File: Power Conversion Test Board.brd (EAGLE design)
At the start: 130 x 112.6 mm, 44 parts, among them U1 LM2678, U2 LM2678

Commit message: lots of things
put in board outline, also fixed the inductors because they were the wrong ones
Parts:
- removed L1, L2, L3, L4: 7.5uH, rcl:L2012C
- removed L5, L6: 15uH, rcl:L2012C
- added U$10, U$7, U$8, U$9: 7.8 uH, DiscreteComponents:HCMA1305
- added U$11, U$6: 15 uH, DiscreteComponents:HCMA1305
- moved U$3 119.1 mm to (78.7, 67.3)
- moved C28 116.3 mm to (72.4, 53.3)
- moved U2 115.6 mm to (44.5, 73.7)
- moved U$4 115.0 mm to (63.5, 92.7)
- moved U1 111.5 mm to (40.6, 88.9)
- moved U$1 77.8 mm to (50.8, 57.1)
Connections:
- net +5V: now also U$6.P$2, U$8.P$2; no longer L1.2, L5.2
- net +5V_3.3V: now also U$11.P$2, U$9.P$2; no longer L3.2, L6.2
- net GND_5V: now also U$7.P$1; no longer L2.1
- net GND_5V3: now also U$10.P$1; no longer L4.1
- net N$1: now also U$6.P$1, U$8.P$1; no longer L1.1, L5.1
- net N$6: now also U$10.P$2; no longer L4.2
- net N$7: now also U$11.P$1, U$9.P$1; no longer L3.1, L6.1
- net N$8: now also U$7.P$2; no longer L2.2
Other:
- board size 130 x 112.6 mm -> 136.7 x 125.3 mm

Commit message: Changed schematic layout and starting routing
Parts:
- C1, C15, C16, C17, C18, C2, C3, C4: device SparkFun-Capacitors:0603 -> SparkFun-Capacitors:1206
- moved U$3 191.4 mm to (-112.7, 65.3), turned to 270 degrees
- moved U2 144.3 mm to (-99.3, 61.5), turned to 270 degrees
- moved U$7 125.2 mm to (-48.0, 67.0)
- moved U$11 124.3 mm to (-20.0, 65.0)
- moved U$10 124.3 mm to (2.00, 45.0)
- moved U$1 109.6 mm to (-50.9, 98.2), turned to 270 degrees
- moved U$4 96.0 mm to (-32.5, 95.7)
- moved U$8 93.3 mm to (4.00, 17.0)
- moved U$6 87.5 mm to (-77.0, 64.0)
- moved U$9 79.2 mm to (-24.0, 4.00)
- moved C1 78.3 mm to (28.4, 80.2)
- moved C8 71.8 mm to (17.9, 15.8)
- moved C28 59.6 mm to (17.4, 30.3)
- moved C7 55.0 mm to (8.01, 30.8)
- moved C19 47.0 mm to (3.76, 95.1)
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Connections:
- net +12V: now also C1.2, C15.2, C16.2, C17.2, C18.2, C19.2, C2.2, C3.2, C4.2, C5.2; no longer C1.1, C15.1, C16.1, C17.1, C18.1, C19.1, C2.1, C3.1, C4.1, C5.1
- net GND: now also C1.1, C15.1, C16.1, C17.1, C18.1, C19.1, C2.1, C3.1, C4.1, C5.1; no longer C1.2, C15.2, C16.2, C17.2, C18.2, C19.2, C2.2, C3.2, C4.2, C5.2

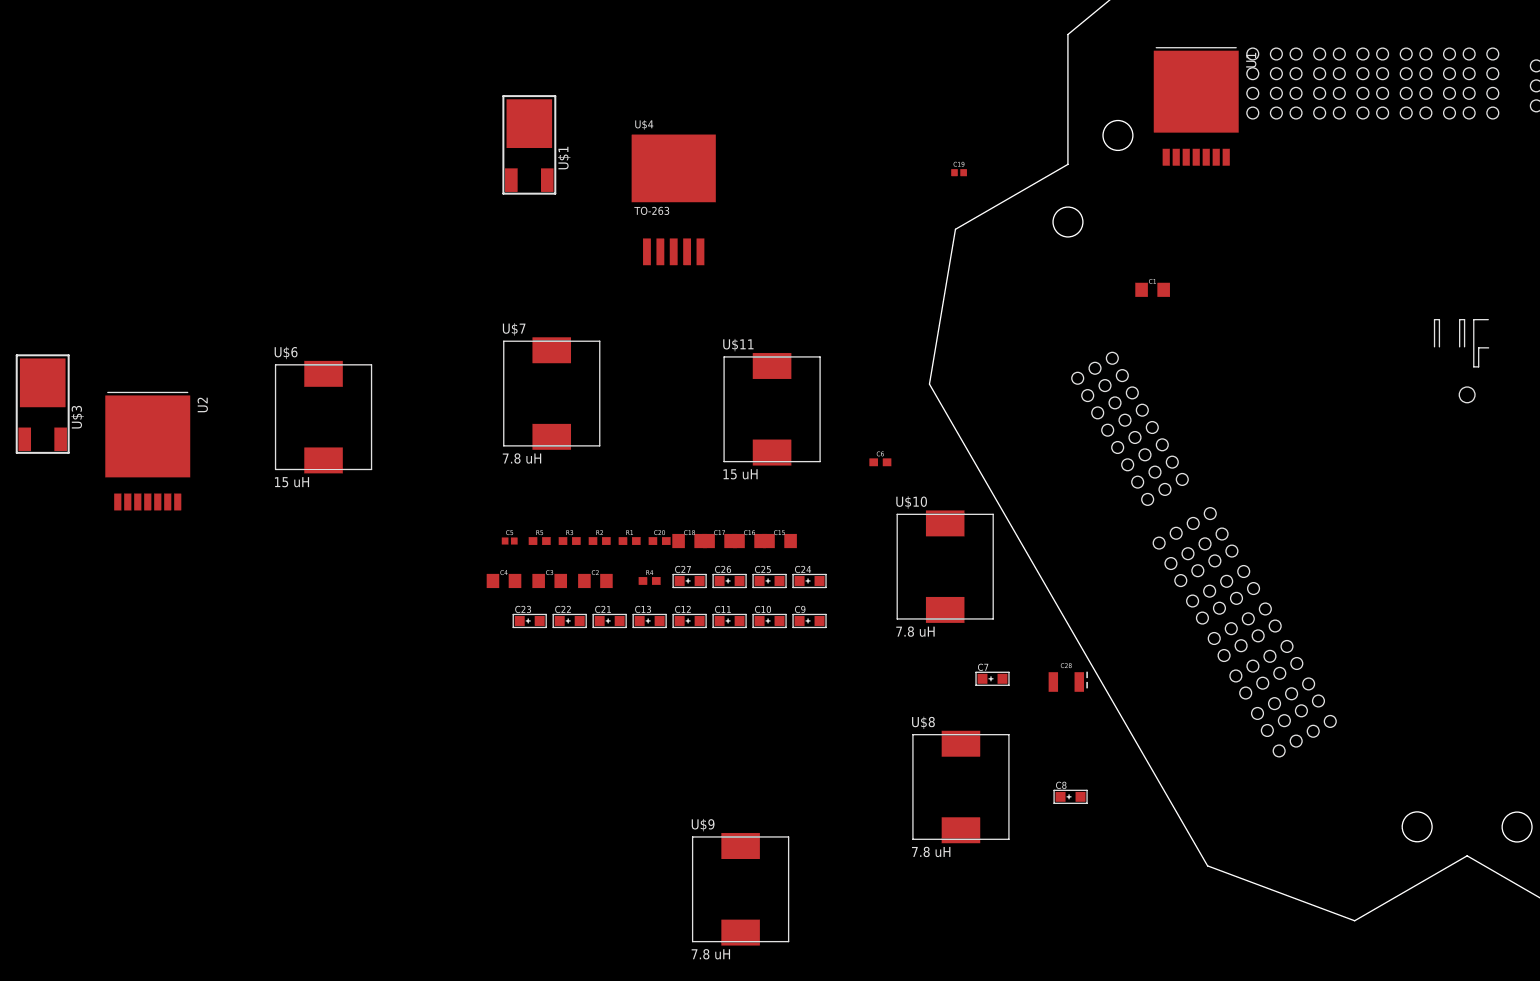
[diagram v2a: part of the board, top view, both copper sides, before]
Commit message: Rerouting
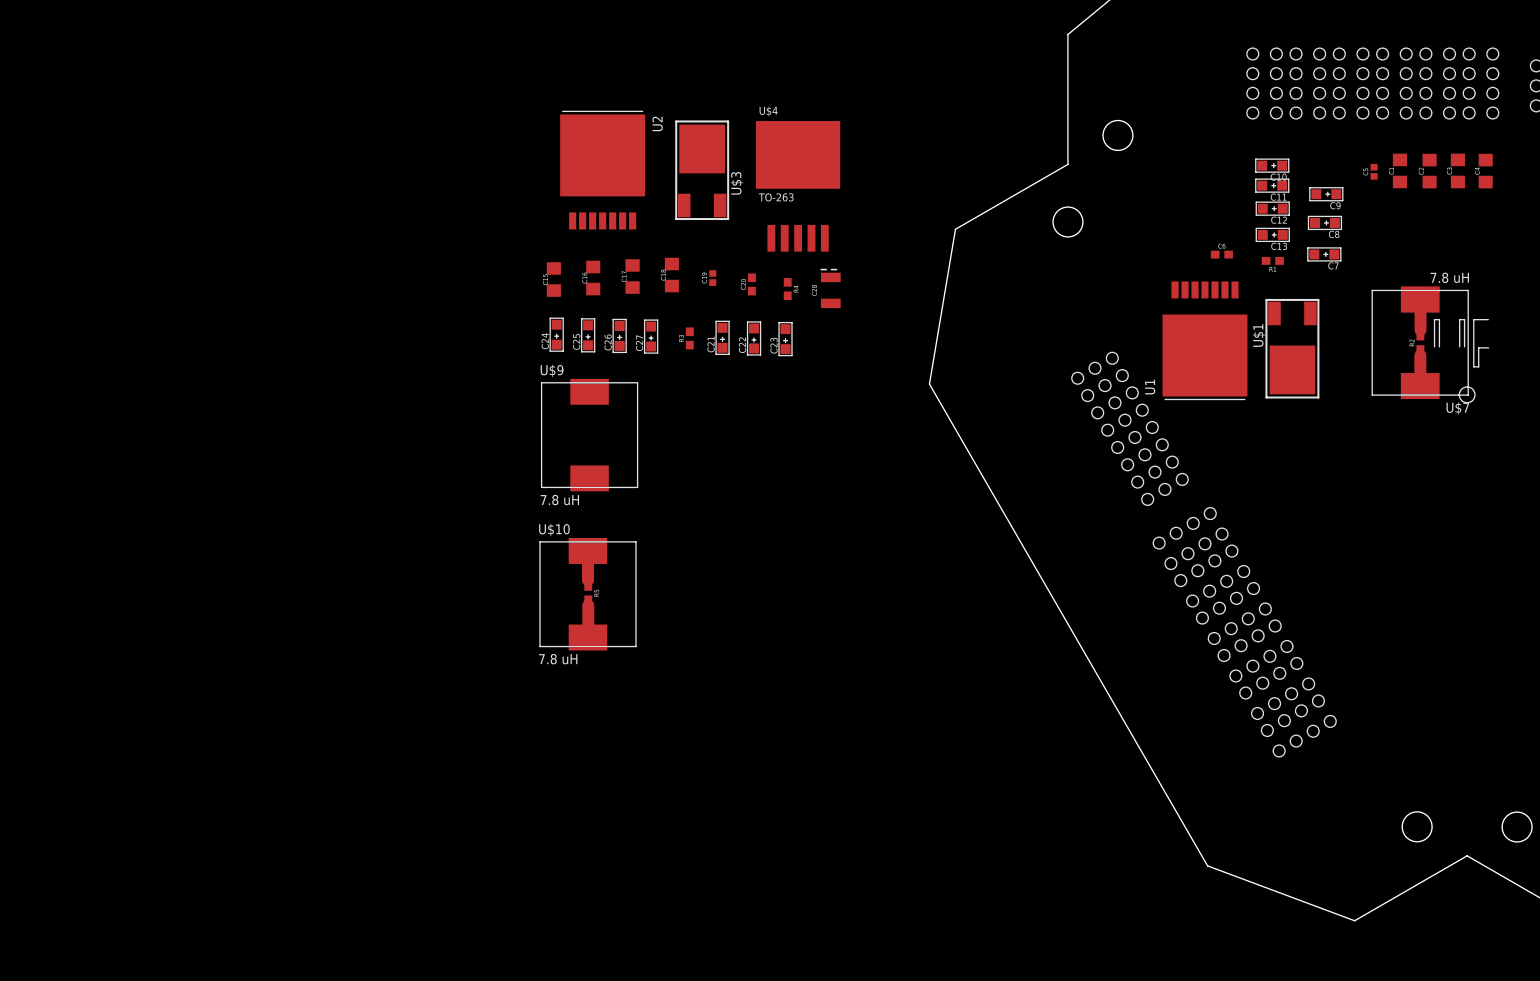
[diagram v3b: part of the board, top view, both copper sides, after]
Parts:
- removed U$11, U$6: 15 uH, DiscreteComponents:HCMA1305
- moved C4 135.2 mm to (70.7, 95.3), turned to 90 degrees
- moved C3 126.6 mm to (67.2, 95.3), turned to 90 degrees
- moved C5 119.4 mm to (56.5, 95.2), turned to 90 degrees
- moved C2 118.1 mm to (63.6, 95.3), turned to 90 degrees
- moved U$7 110.6 mm to (62.4, 73.5), turned to 180 degrees
- moved R2 107.3 mm to (62.4, 73.4), turned to 90 degrees
- moved U$1 100.2 mm to (46.1, 73.1), turned to 90 degrees
- moved C13 93.2 mm to (43.6, 87.2), turned to 180 degrees
- moved C12 90.8 mm to (43.6, 90.5), turned to 180 degrees
- moved R1 89.1 mm to (43.6, 83.9), turned to 180 degrees
- moved U$3 88.9 mm to (-28.9, 95.0)
- moved C11 88.4 mm to (43.6, 93.4), turned to 180 degrees
- moved C10 86.2 mm to (43.6, 96.0), turned to 180 degrees
- moved C9 85.2 mm to (50.4, 92.3), turned to 180 degrees
- moved U$8 81.2 mm to (62.4, 73.5), flipped to the bottom, turned to 180 degrees
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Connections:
- removed net GND_5V1: R5.1
- removed net N$6: C21.-, C22.-, C23.-, U$10.P$2
- net +5V: no longer U$6.P$2
- net +5V_3.3V: no longer U$11.P$2
- net GND_5V3: now also R5.1
- net N$1: no longer U$6.P$1
- net N$4: now also C21.-, C22.-, C23.-, U$10.P$2
- net N$7: no longer U$11.P$1
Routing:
- net N$4: track 0.00 -> 4.81 mm
- net GND_5V: track 0.00 -> 4.69 mm
- net N$8: track 0.00 -> 4.68 mm
- net GND_5V3: track 0.00 -> 4.53 mm

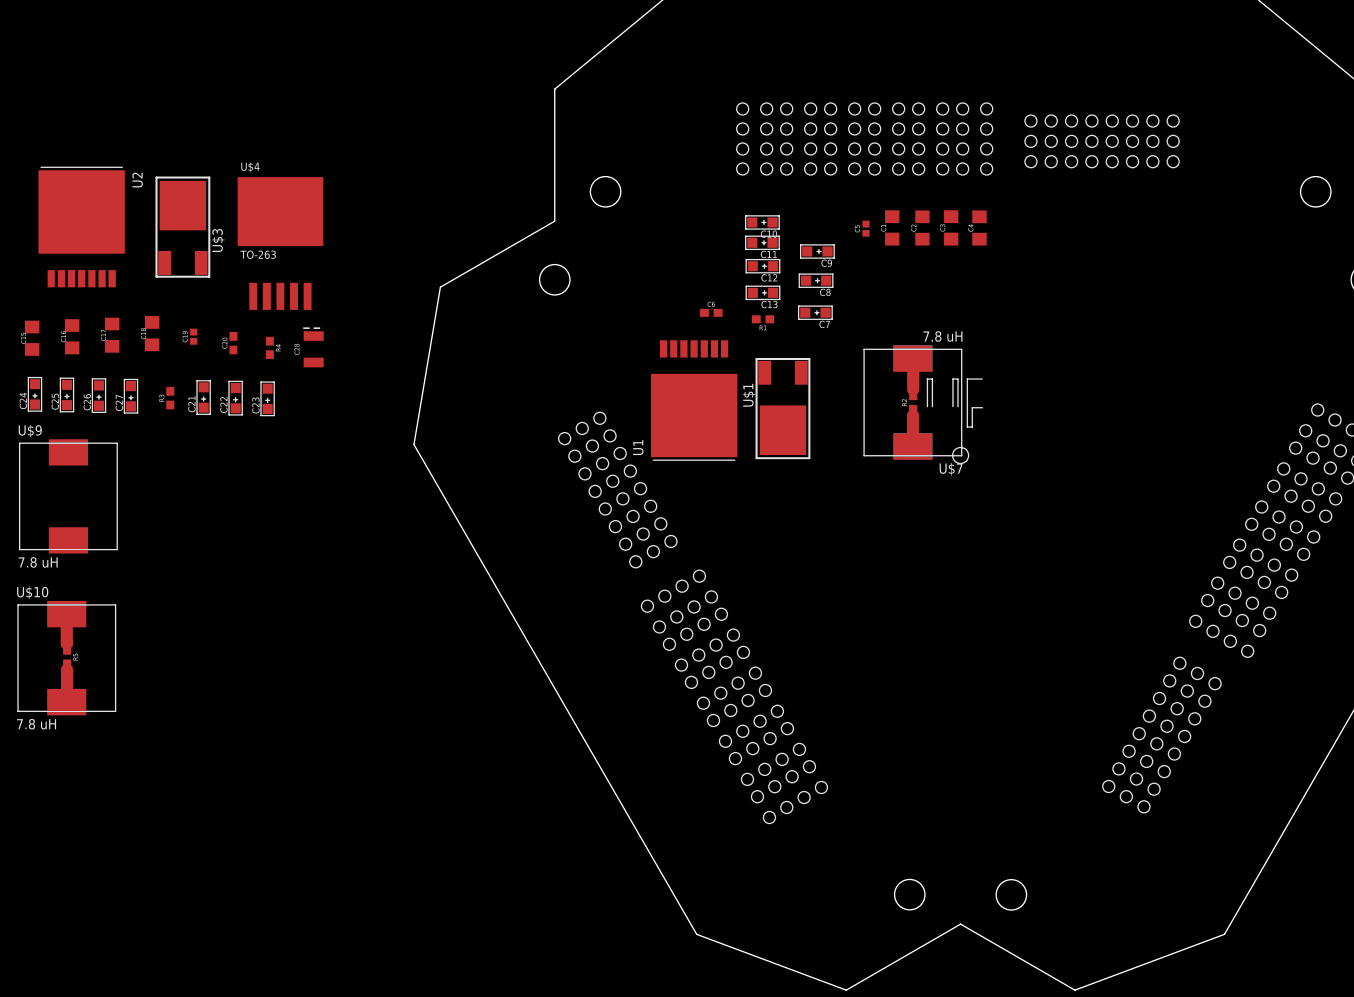
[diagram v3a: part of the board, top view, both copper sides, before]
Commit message: Repositioned the components of the board to get ready for tracing
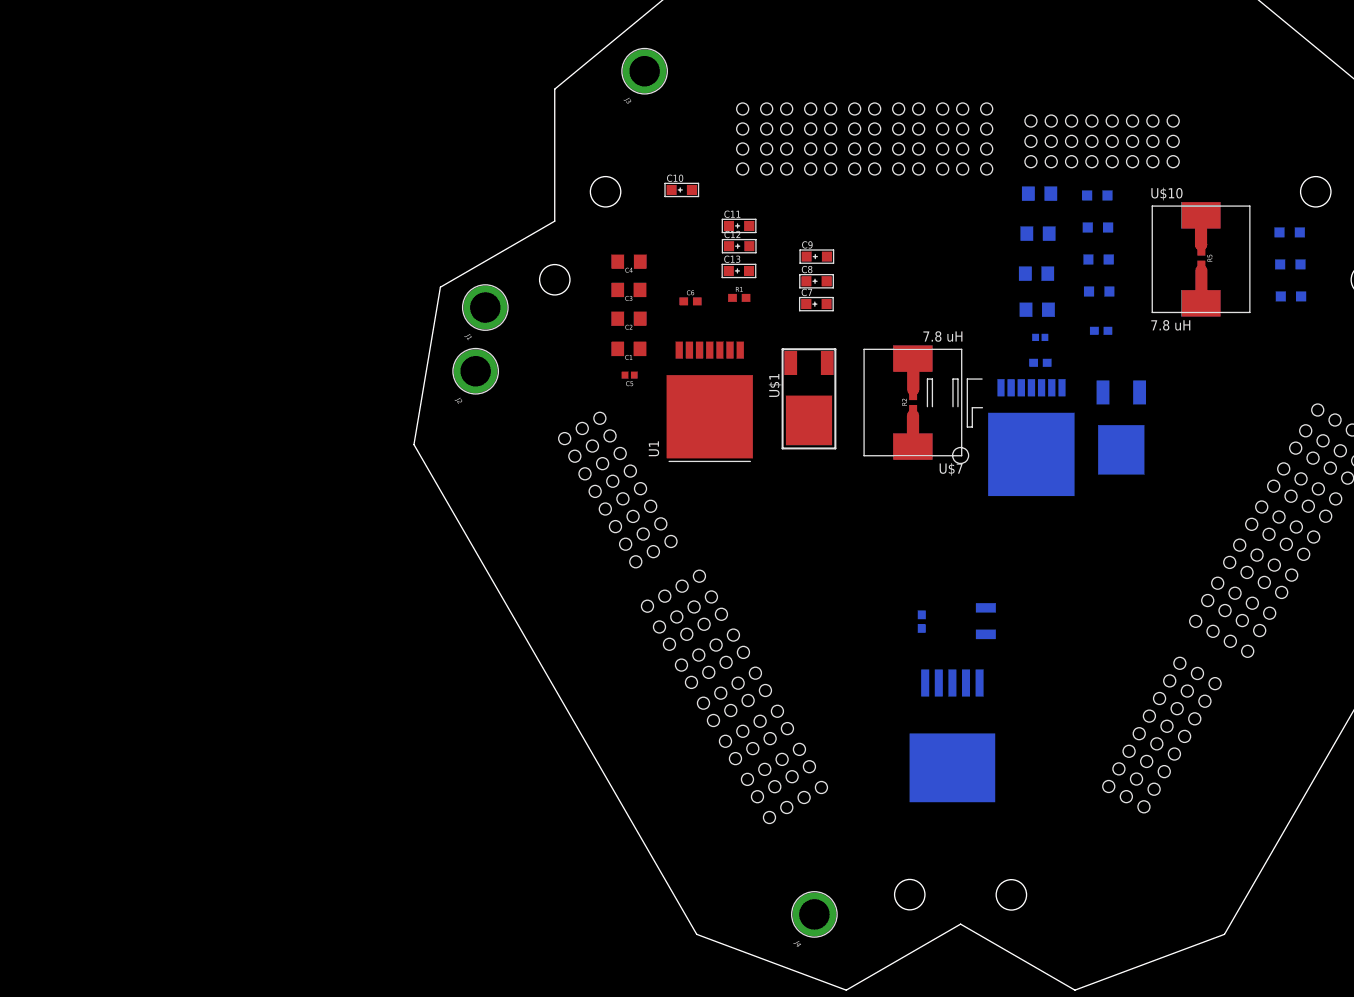
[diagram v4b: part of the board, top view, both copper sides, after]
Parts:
- added J1, J2, J3, J4: (no value), SparkFun-Connectors:BANANA_CONN
- moved R5 150.3 mm to (98.4, 91.5)
- moved U$10 150.3 mm to (98.4, 91.4)
- moved U$9 144.6 mm to (98.3, 91.3), flipped to the bottom, turned to 180 degrees
- moved C21 137.3 mm to (109.5, 94.7), flipped to the bottom, turned to 0 degrees
- moved C24 135.1 mm to (85.4, 99.3), flipped to the bottom, turned to 0 degrees
- moved C22 132.9 mm to (109.5, 90.7), flipped to the bottom, turned to 0 degrees
- moved C25 130.6 mm to (85.5, 95.3), flipped to the bottom, turned to 0 degrees
- moved C23 128.6 mm to (109.6, 86.7), flipped to the bottom, turned to 0 degrees
- moved C15 127.2 mm to (78.2, 99.6), flipped to the bottom, turned to 0 degrees
- moved C26 126.1 mm to (85.6, 91.3), flipped to the bottom, turned to 0 degrees
- moved U2 122.5 mm to (77.2, 67.0), flipped to the bottom, turned to 90 degrees
- moved C27 121.7 mm to (85.7, 87.3), flipped to the bottom, turned to 0 degrees
- moved C16 121.4 mm to (78.0, 94.6), flipped to the bottom, turned to 0 degrees
- moved U$3 119.8 mm to (88.4, 70.6), flipped to the bottom, turned to 90 degrees
- moved R3 116.7 mm to (85.9, 82.4), flipped to the bottom, turned to 0 degrees
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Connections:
- removed net GND: C1.1, C10.+, C11.+, C12.+, C13.+, C15.1, C16.1, C17.1, C18.1, C19.1, C2.1, C24.+, C25.+, C26.+, C27.+, C3.1, C4.1, C5.1, R1.1, R3.1, U1.4, U1.TAB
- removed net GND_5V: C10.-, C11.-, C12.-, C13.-, R1.2, R2.1, U$1.P$1, U$1.P$3, U$7.P$1
- removed net GND_5V3: C24.-, C25.-, C26.-, C27.-, R3.2, R5.1, U$10.P$1, U$3.P$1, U$3.P$3, U2.4, U2.TAB
- removed net N$9: R4.1, U$4.P$3, U$4.P$6
- new net 12VGND: C1.1, C10.+, C11.+, C12.+, C13.+, C2.1, C3.1, C4.1, C5.1, J2.P$1, R1.1, U1.4, U1.TAB
- new net 3.3VGND: J4.P$1, R4.1, U$4.P$3, U$4.P$6
- new net 5VGND: C10.-, C11.-, C12.-, C13.-, C24.-, C25.-, C26.-, C27.-, J3.P$1, R1.2, R2.1, R3.2, R5.1, U$1.P$1, U$1.P$3, U$10.P$1, U$3.P$1, U$3.P$3, U$7.P$1, U2.4, U2.TAB
- new net N$6: C15.1, C16.1, C17.1, C18.1, C19.1, C24.+, C25.+, C26.+, C27.+, R3.1
- net +12V: now also J1.P$1
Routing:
- net 5VGND: track 0.00 -> 9.21 mm
- net GND_5V: track 4.69 -> 0.00 mm
- net GND_5V3: track 4.53 -> 0.00 mm

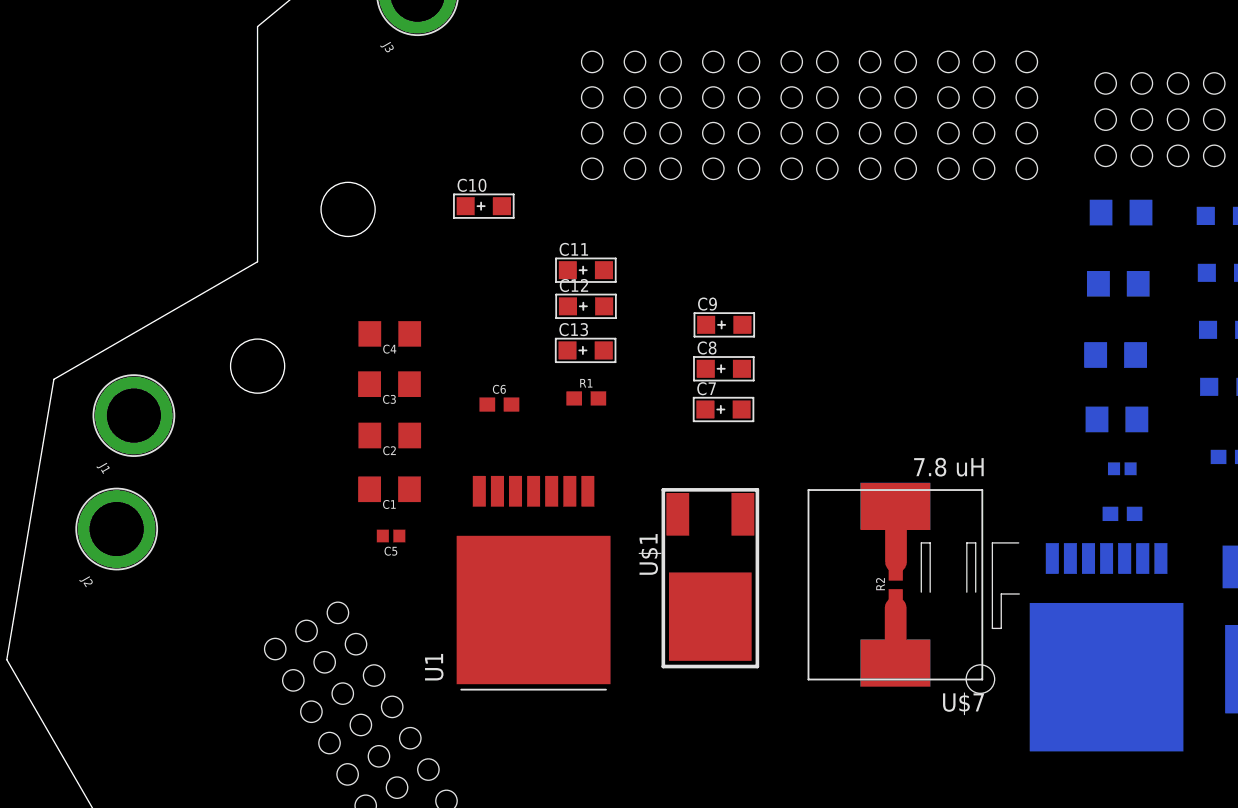
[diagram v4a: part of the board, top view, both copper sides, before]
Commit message: re-positioned parts
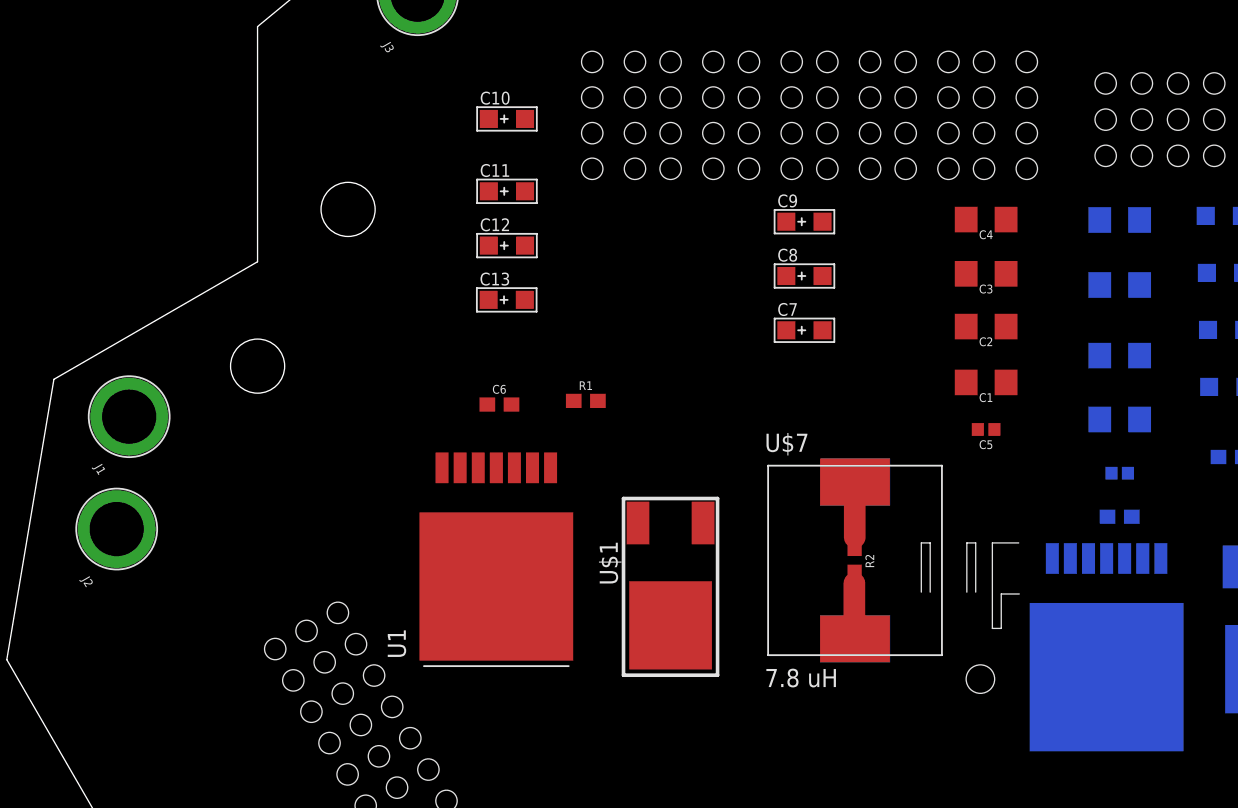
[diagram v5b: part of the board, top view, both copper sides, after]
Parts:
- moved C4 42.6 mm to (68.7, 99.1)
- moved C3 42.6 mm to (68.7, 95.3)
- moved C2 42.5 mm to (68.7, 91.6)
- moved C1 42.5 mm to (68.7, 87.7)
- moved C5 42.4 mm to (68.7, 84.4)
- moved C9 9.17 mm to (56.0, 98.9)
- moved C8 8.63 mm to (56.0, 95.1)
- moved C7 7.95 mm to (56.0, 91.3)
- moved C11 7.83 mm to (35.1, 101.1)
- moved C12 7.00 mm to (35.1, 97.3)
- moved C13 6.58 mm to (35.1, 93.4)
- moved C10 6.33 mm to (35.1, 106.1)
- moved R2 3.36 mm to (59.5, 75.2), turned to 270 degrees
- moved U$7 3.31 mm to (59.5, 75.2), turned to 0 degrees
- moved U$8 3.29 mm to (59.5, 75.2)
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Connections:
- removed net N$6: C15.1, C16.1, C17.1, C18.1, C19.1, C24.+, C25.+, C26.+, C27.+, R3.1
- net 12VGND: now also C15.1, C16.1, C17.1, C18.1, C19.1, C24.+, C25.+, C26.+, C27.+, R3.1
